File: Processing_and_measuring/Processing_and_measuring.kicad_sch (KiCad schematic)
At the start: 38 parts, among them J1 Conn_02x07_Counter_Clockwise, J2 Conn_01x02_Pin, J3 Conn_02x07_Counter_Clockwise, J4 Conn_01x04_Pin, U1 TPL7407LAD, U2 CD74HC4067M, U3 AVR128DA48x-xPT, U4 TPL7407LAD, Y1 X_Crystal_16MHz_18pF

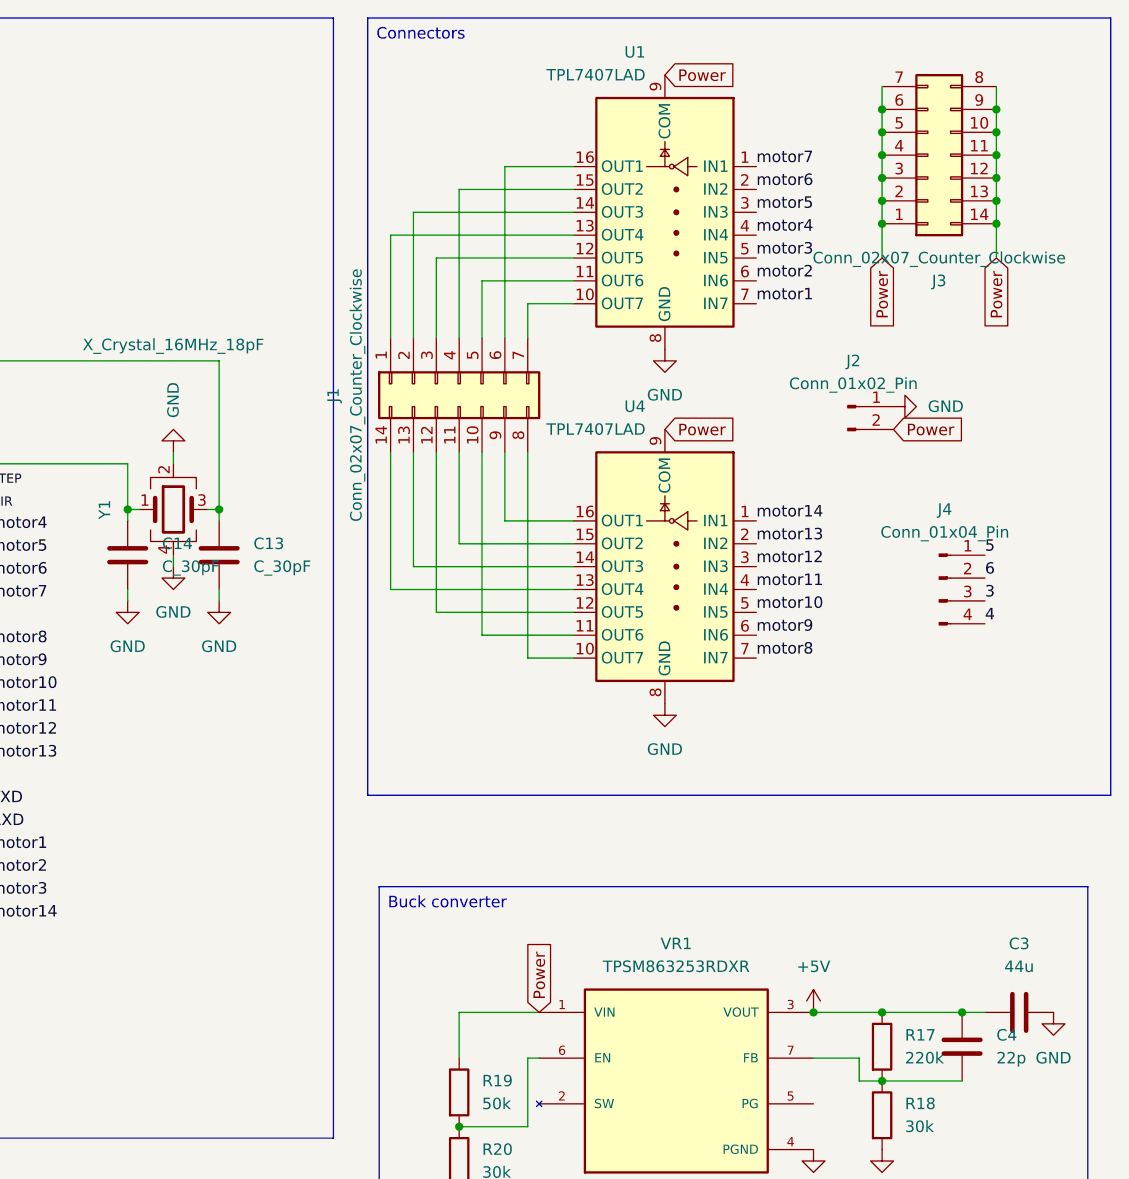
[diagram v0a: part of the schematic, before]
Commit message: Updated capacitors and added button connector
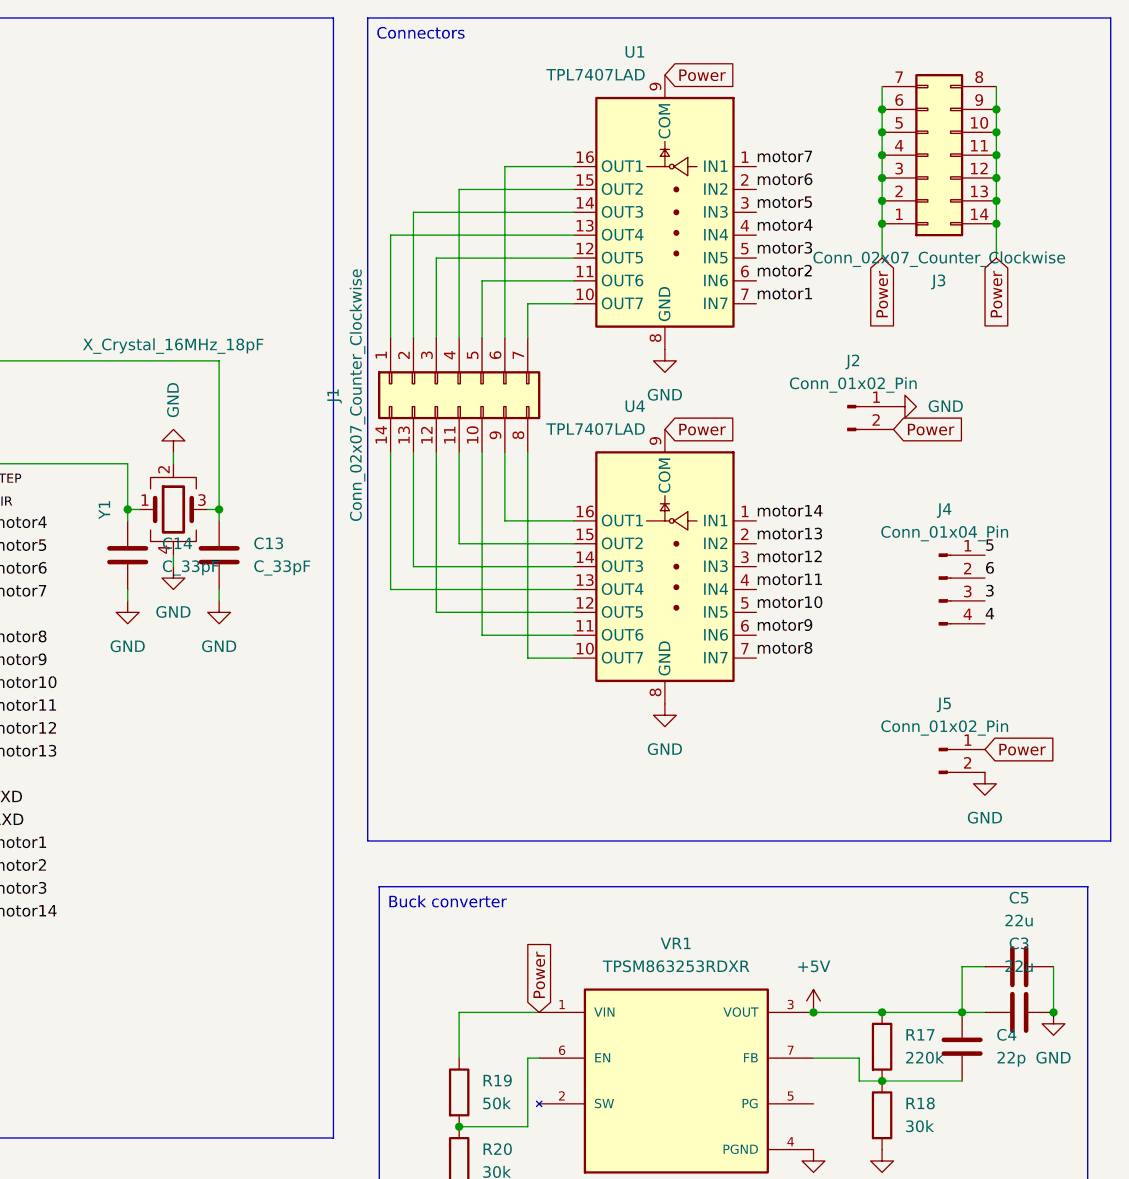
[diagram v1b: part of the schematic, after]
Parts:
- added C5: 22u, Capacitor_SMD:C_0603_1608Metric, symbol Device:C
- added J5: Conn_01x02_Pin, Connector_PinHeader_1.00mm:PinHeader_1x02_P1.00mm_Horizontal, symbol Connector:Conn_01x02_Pin
- C13, C14: value C_30pF -> C_33pF
- C3: value 44u -> 22u
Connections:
- net +5V: now also C5.1
- net GND: now also C5.2, J5.2 (Pin_2)
- net Power: now also J5.1 (Pin_1)

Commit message: Lots of progress made on assembly
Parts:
- added J6: Conn_01x02_Pin, Connector_PinHeader_1.00mm:PinHeader_1x02_P1.00mm_Horizontal, symbol Connector:Conn_01x02_Pin
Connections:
- net 3: now also A1.3 (1B)
- net 4: now also A1.4 (1A)
- net 5: now also A1.5 (2A)
- net 6: now also A1.6 (2B)
- net Power: now also A1.8 (VMOT)
- net RXD: now also J6.2 (Pin_2)
- net TXD: now also J6.1 (Pin_1)
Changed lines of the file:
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@@
+		)
+	)
+	(label "4"
+		(at 72.39 156.21 0)
+		(effects
+			(font
+				(size 1.27 1.27)
+			)
+			(justify left bottom)
 		)
 	)
@@
 		)
 	)
+	(label "6"
+		(at 72.39 161.29 0)
+		(effects
+			(font
+				(size 1.27 1.27)
+			)
+			(justify left bottom)
+		)
+	)
 	(label "4"
 		(at 269.24 83.82 0)
@@
 		)
 	)
+	(label "TXD"
+		(at 217.17 101.6 0)
+		(effects
+			(font
+				(size 1.27 1.27)
+			)
+			(justify left bottom)
+		)
+	)
 	(label "motor4"
 		(at 243.84 40.64 0)
@@
 		)
 	)
+	(label "RXD"
+		(at 217.17 104.14 0)
+		(effects
+			(font
+				(size 1.27 1.27)
+			)
+			(justify left bottom)
+		)
+	)
 	(label "motor12"
 		(at 158.75 96.52 0)
@@
 		)
 	)
+	(label "5"
+		(at 72.39 158.75 0)
+		(effects
+			(font
+				(size 1.27 1.27)
+			)
+			(justify left bottom)
+		)
+	)
 	(label "motor14"
 		(at 158.75 116.84 0)
@@
 	(label "TXD"
 		(at 158.75 104.14 0)
+		(effects
+			(font
+				(size 1.27 1.27)
+			)
+			(justify left bottom)
+		)
+	)
+	(label "3"
+		(at 72.39 153.67 0)
 		(effects
 			(font
@@
 		(property "Intersheetrefs" "${INTERSHEET_REFS}"
 			(at 219.71 118.3905 90)
+			(effects
+				(font
+					(size 1.27 1.27)
+				)
+				(justify left)
+				(hide yes)
+			)
+		)
+	)
+	(global_label "Power"
+		(shape input)
+		(at 64.77 138.43 90)
+		(fields_autoplaced yes)
+		(effects
+			(font
+				(size 1.27 1.27)
+			)
+			(justify left)
+		)
+		(property "Intersheetrefs" "${INTERSHEET_REFS}"
+			(at 64.77 129.8205 90)
 			(effects
 				(font
@@
 					(unit 1)
 				)
+			)
+		)
+	)
+	(symbol
+		(lib_id "Connector:Conn_01x02_Pin")
+		(at 212.09 101.6 0)
+		(unit 1)
+		(exclude_from_sim no)
+		(in_bom yes)
+		(on_board yes)
+		(dnp no)
+		(fields_autoplaced yes)
+		(property "Reference" "J6"
+			(at 212.725 96.52 0)
+			(effects
+				(font
+					(size 1.27 1.27)
+				)
+			)
+		)
+		(property "Value" "Conn_01x02_Pin"
+			(at 212.725 99.06 0)
+			(effects
+				(font
+					(size 1.27 1.27)
+				)
+			)
+		)
+		(property "Footprint" "Connector_PinHeader_1.00mm:PinHeader_1x02_P1.00mm_Horizontal"
+			(at 212.09 101.6 0)
+			(effects
+				(font
+					(size 1.27 1.27)
+				)
+				(hide yes)
+			)
+		)
+		(property "Datasheet" "~"
+			(at 212.09 101.6 0)
+			(effects
+				(font
+					(size 1.27 1.27)
+				)
+				(hide yes)
+			)
+		)
+		(property "Description" "Generic connector, single row, 01x02, script generated"
+			(at 212.09 101.6 0)
+			(effects
+				(font
+					(size 1.27 1.27)
+				)
+				(hide yes)
+			)
+		)
+		(pin "2"
+		)
+		(pin "1"
+		)
+		(instances
+			(project "Processing_and_measuring"
+				(path "/042b9f46-6dbb-45f9-91f7-21f14ba1e222"
+					(reference "J6")
+					(unit 1)
+				)

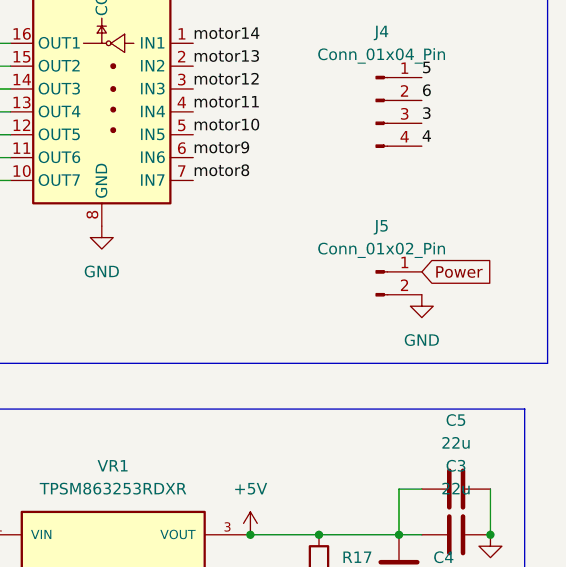
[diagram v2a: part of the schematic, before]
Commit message: Buck converter layout mostly
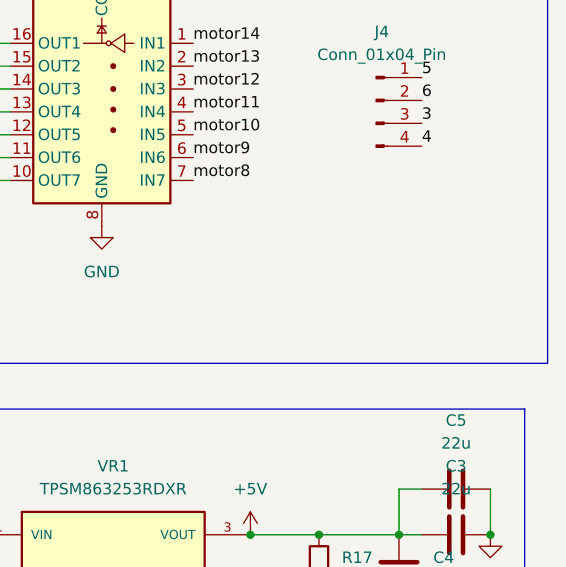
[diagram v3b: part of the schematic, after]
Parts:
- removed J5: Conn_01x02_Pin, Connector_PinHeader_1.00mm:PinHeader_1x02_P1.00mm_Horizontal, symbol Connector:Conn_01x02_Pin
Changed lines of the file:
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@@
 	(global_label "Power"
 		(shape input)
-		(at 269.24 97.79 0)
-		(fields_autoplaced yes)
-		(effects
-			(font
-				(size 1.27 1.27)
-			)
-			(justify left)
-		)
-		(property "Intersheetrefs" "${INTERSHEET_REFS}"
-			(at 277.8495 97.79 0)
-			(effects
-				(font
-					(size 1.27 1.27)
-				)
-				(justify left)
-				(hide yes)
-			)
-		)
-	)
-	(global_label "Power"
-		(shape input)
 		(at 233.68 62.23 0)
 		(fields_autoplaced yes)
@@
 	)
 	(symbol
-		(lib_id "power:GND")
-		(at 269.24 100.33 0)
-		(unit 1)
-		(exclude_from_sim no)
-		(in_bom yes)
-		(on_board yes)
-		(dnp no)
-		(fields_autoplaced yes)
-		(property "Reference" "#PWR022"
-			(at 269.24 106.68 0)
-			(effects
-				(font
-					(size 1.27 1.27)
-				)
-				(hide yes)
-			)
-		)
-		(property "Value" "GND"
-			(at 269.24 105.41 0)
-			(effects
-				(font
-					(size 1.27 1.27)
-				)
-			)
-		)
-		(property "Footprint" ""
-			(at 269.24 100.33 0)
-			(effects
-				(font
-					(size 1.27 1.27)
-				)
-				(hide yes)
-			)
-		)
-		(property "Datasheet" ""
-			(at 269.24 100.33 0)
-			(effects
-				(font
-					(size 1.27 1.27)
-				)
-				(hide yes)
-			)
-		)
-		(property "Description" "Power symbol creates a global label with name \"GND\" , ground"
-			(at 269.24 100.33 0)
-			(effects
-				(font
-					(size 1.27 1.27)
-				)
-				(hide yes)
-			)
-		)
-		(pin "1"
-		)
-		(instances
-			(project "Processing_and_measuring"
-				(path "/042b9f46-6dbb-45f9-91f7-21f14ba1e222"
-					(reference "#PWR022")
-					(unit 1)
-				)
-			)
-		)
-	)
-	(symbol
 		(lib_id "Device:R")
 		(at 71.12 85.09 90)
@@
 			)
 		)
-		(property "Datasheet" ""
+		(property "Datasheet" "https://www.ti.com/lit/ds/symlink/tpsm863253.pdf?ts=1707940480558&ref_url=https%253A%252F%252Fwww.ti.com%252Fproduct%252FTPSM863253"
 			(at 234.95 134.62 0)
 			(effects
@@
 					(unit 1)
 				)
-			)
-		)
-	)
-	(symbol
-		(lib_id "Connector:Conn_01x02_Pin")
-		(at 264.16 97.79 0)
-		(unit 1)
-		(exclude_from_sim no)
-		(in_bom yes)
-		(on_board yes)
-		(dnp no)
-		(fields_autoplaced yes)
-		(property "Reference" "J5"
-			(at 264.795 92.71 0)
-			(effects
-				(font
-					(size 1.27 1.27)
-				)
-			)
-		)
-		(property "Value" "Conn_01x02_Pin"
-			(at 264.795 95.25 0)
-			(effects
-				(font
-					(size 1.27 1.27)
-				)
-			)
-		)
-		(property "Footprint" "Connector_PinHeader_1.00mm:PinHeader_1x02_P1.00mm_Horizontal"
-			(at 264.16 97.79 0)
-			(effects
-				(font
-					(size 1.27 1.27)
-				)
-				(hide yes)
-			)
-		)
-		(property "Datasheet" "~"
-			(at 264.16 97.79 0)
-			(effects
-				(font
-					(size 1.27 1.27)
-				)
-				(hide yes)
-			)
-		)
-		(property "Description" "Generic connector, single row, 01x02, script generated"
-			(at 264.16 97.79 0)
-			(effects
-				(font
-					(size 1.27 1.27)
-				)
-				(hide yes)
-			)
-		)
-		(pin "2"
-		)
-		(pin "1"
-		)
-		(instances
-			(project ""
-				(path "/042b9f46-6dbb-45f9-91f7-21f14ba1e222"
-					(reference "J5")
-					(unit 1)
-				)

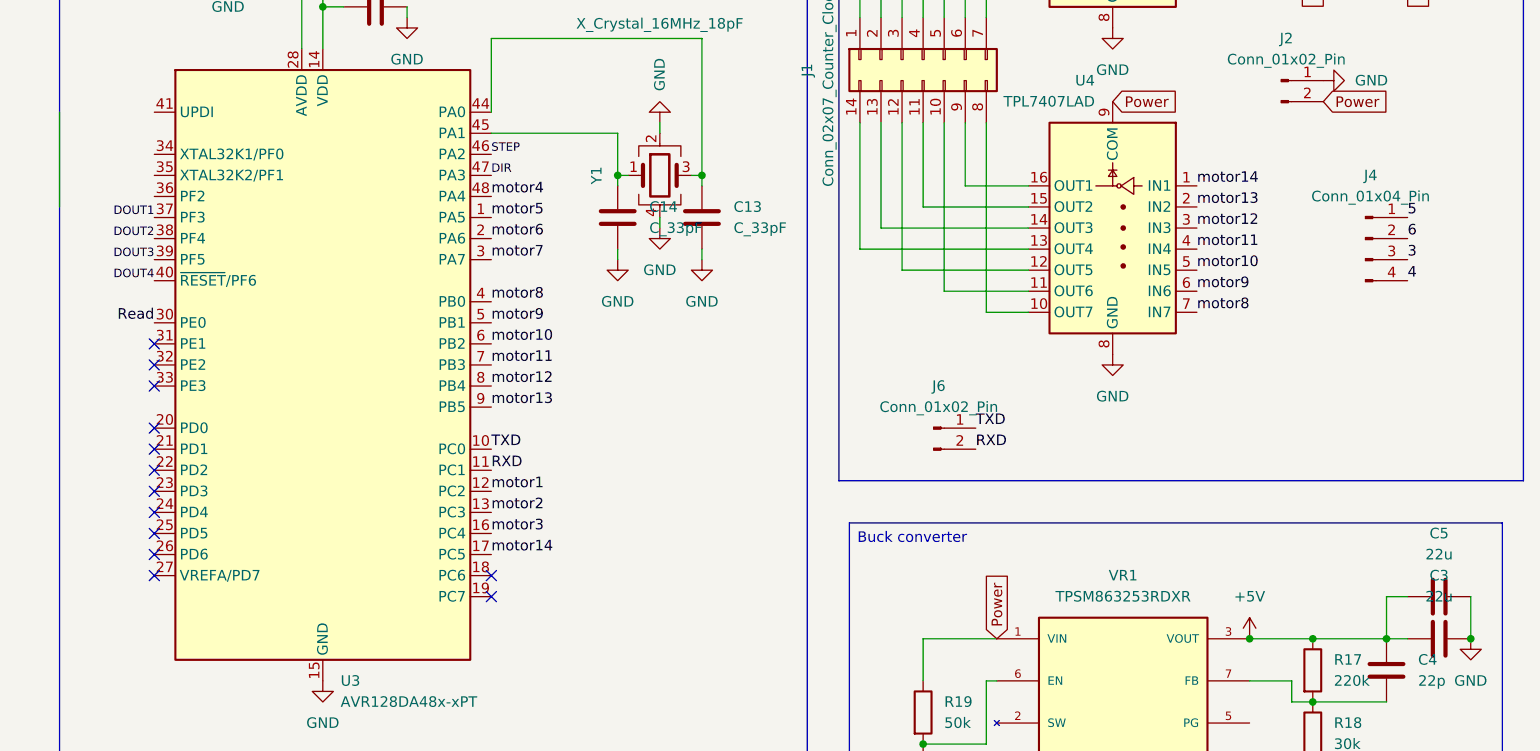
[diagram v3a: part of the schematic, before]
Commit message: added button to mcu
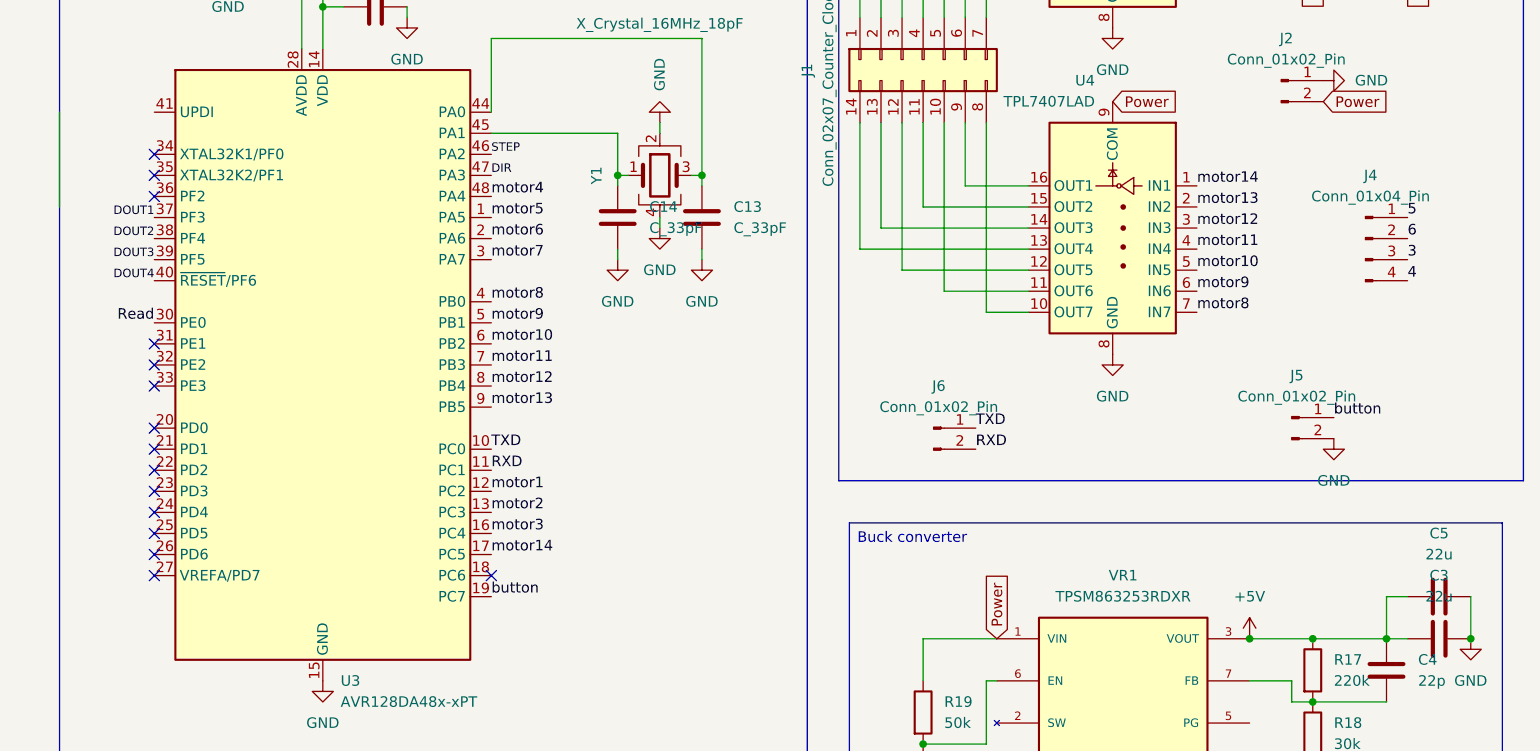
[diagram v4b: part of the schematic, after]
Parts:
- added J5: Conn_01x02_Pin, Connector_PinHeader_1.00mm:PinHeader_1x02_P1.00mm_Horizontal, symbol Connector:Conn_01x02_Pin
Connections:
- net GND: now also J5.2 (Pin_2)
- net button: now reaches U3.19 (PC7)
- net button: now also J5.1 (Pin_1)
- no-connect marks 13 -> 15
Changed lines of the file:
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@@
 	)
 	(no_connect
-		(at 158.75 119.38)
+		(at 118.11 68.58)
 	)
 	(no_connect
@@
 	)
 	(no_connect
-		(at 158.75 121.92)
+		(at 118.11 71.12)
 	)
 	(no_connect
@@
 	)
 	(no_connect
+		(at 158.75 119.38)
+	)
+	(no_connect
+		(at 118.11 73.66)
+	)
+	(no_connect
 		(at 118.11 119.38)
 	)
@@
 		)
 	)
+	(label "button"
+		(at 260.35 100.33 0)
+		(effects
+			(font
+				(size 1.27 1.27)
+			)
+			(justify left bottom)
+		)
+	)
 	(label "RXD"
 		(at 158.75 106.68 0)
@@
 		)
 	)
+	(label "button"
+		(at 158.75 121.92 0)
+		(effects
+			(font
+				(size 1.27 1.27)
+			)
+			(justify left bottom)
+		)
+	)
 	(label "3"
 		(at 269.24 81.28 0)
@@
 	)
 	(symbol
+		(lib_id "power:GND")
+		(at 260.35 102.87 0)
+		(unit 1)
+		(exclude_from_sim no)
+		(in_bom yes)
+		(on_board yes)
+		(dnp no)
+		(fields_autoplaced yes)
+		(property "Reference" "#PWR022"
+			(at 260.35 109.22 0)
+			(effects
+				(font
+					(size 1.27 1.27)
+				)
+				(hide yes)
+			)
+		)
+		(property "Value" "GND"
+			(at 260.35 107.95 0)
+			(effects
+				(font
+					(size 1.27 1.27)
+				)
+			)
+		)
+		(property "Footprint" ""
+			(at 260.35 102.87 0)
+			(effects
+				(font
+					(size 1.27 1.27)
+				)
+				(hide yes)
+			)
+		)
+		(property "Datasheet" ""
+			(at 260.35 102.87 0)
+			(effects
+				(font
+					(size 1.27 1.27)
+				)
+				(hide yes)
+			)
+		)
+		(property "Description" "Power symbol creates a global label with name \"GND\" , ground"
+			(at 260.35 102.87 0)
+			(effects
+				(font
+					(size 1.27 1.27)
+				)
+				(hide yes)
+			)
+		)
+		(pin "1"
+		)
+		(instances
+			(project "Processing_and_measuring"
+				(path "/042b9f46-6dbb-45f9-91f7-21f14ba1e222"
+					(reference "#PWR022")
+					(unit 1)
+				)
+			)
+		)
+	)
+	(symbol
 		(lib_id "Device:R")
 		(at 71.12 62.23 90)
@@
 					(unit 1)
 				)
+			)
+		)
+	)
+	(symbol
+		(lib_id "Connector:Conn_01x02_Pin")
+		(at 255.27 100.33 0)
+		(unit 1)
+		(exclude_from_sim no)
+		(in_bom yes)
+		(on_board yes)
+		(dnp no)
+		(fields_autoplaced yes)
+		(property "Reference" "J5"
+			(at 255.905 95.25 0)
+			(effects
+				(font
+					(size 1.27 1.27)
+				)
+			)
+		)
+		(property "Value" "Conn_01x02_Pin"
+			(at 255.905 97.79 0)
+			(effects
+				(font
+					(size 1.27 1.27)
+				)
+			)
+		)
+		(property "Footprint" "Connector_PinHeader_1.00mm:PinHeader_1x02_P1.00mm_Horizontal"
+			(at 255.27 100.33 0)
+			(effects
+				(font
+					(size 1.27 1.27)
+				)
+				(hide yes)
+			)
+		)
+		(property "Datasheet" "~"
+			(at 255.27 100.33 0)
+			(effects
+				(font
+					(size 1.27 1.27)
+				)
+				(hide yes)
+			)
+		)
+		(property "Description" "Generic connector, single row, 01x02, script generated"
+			(at 255.27 100.33 0)
+			(effects
+				(font
+					(size 1.27 1.27)
+				)
+				(hide yes)
+			)
+		)
+		(pin "2"
+		)
+		(pin "1"
+		)
+		(instances
+			(project "Processing_and_measuring"
+				(path "/042b9f46-6dbb-45f9-91f7-21f14ba1e222"
+					(reference "J5")
+					(unit 1)
+				)
